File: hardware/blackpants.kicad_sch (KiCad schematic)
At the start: 26 parts, among them J1 Conn_01x08, J2 Conn_01x10, J3 Conn_ARM_SWD_TagConnect_TC203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, SW1 SW_Push, U1 STM32F042C6Ux, U11 TPSGM7227YUWQ10G

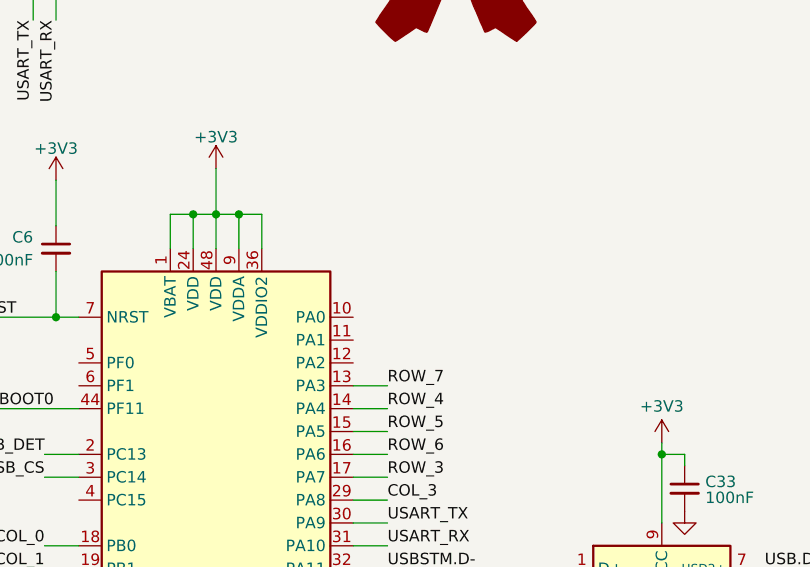
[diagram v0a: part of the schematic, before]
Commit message: Removed old readme, added files.
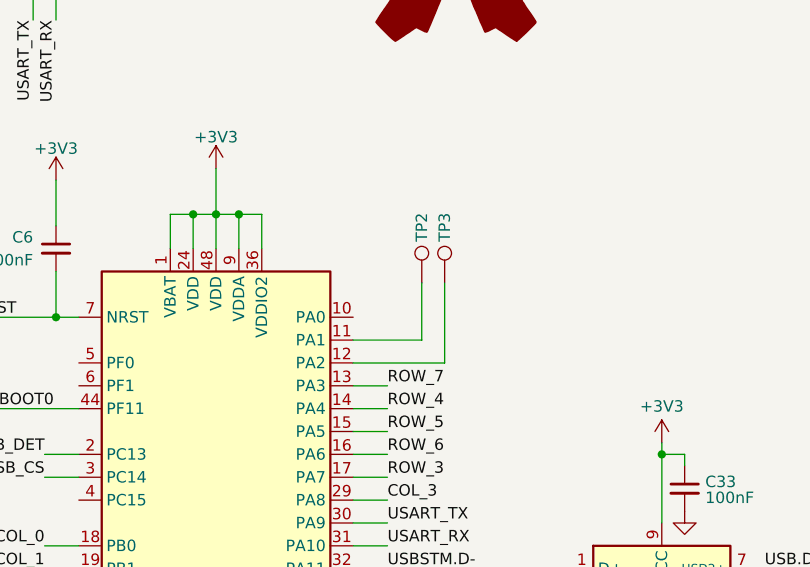
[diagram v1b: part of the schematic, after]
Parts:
- added TP2, TP3: TestPoint, TestPoint:TestPoint_Pad_1.0x1.0mm, symbol Connector:TestPoint
- C7: MPN CL05B104KB54PNC -> CL05B105KQ5NQNC
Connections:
- net at U1.11 (PA1): now also TP2.1
- net at U1.12 (PA2): now also TP3.1
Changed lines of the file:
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@@
 	(wire
 		(pts
+			(xy 156.21 88.9) (xy 156.21 80.01)
+		)
+		(stroke
+			(width 0)
+			(type default)
+		)
+	)
+	(wire
+		(pts
 			(xy 259.08 148.59) (xy 261.62 148.59)
 		)
@@
 	(wire
 		(pts
+			(xy 153.67 86.36) (xy 146.05 86.36)
+		)
+		(stroke
+			(width 0)
+			(type default)
+		)
+	)
+	(wire
+		(pts
 			(xy 190.5 114.3) (xy 200.66 114.3)
 		)
@@
 		)
 	)
+	(wire
+		(pts
+			(xy 146.05 88.9) (xy 156.21 88.9)
+		)
+		(stroke
+			(width 0)
+			(type default)
+		)
+	)
 	(bus
 		(pts
@@
 	(wire
 		(pts
+			(xy 153.67 80.01) (xy 153.67 86.36)
+		)
+		(stroke
+			(width 0)
+			(type default)
+		)
+	)
+	(wire
+		(pts
 			(xy 146.05 93.98) (xy 149.86 93.98)
 		)
@@
 	)
 	(symbol
+		(lib_id "Connector:TestPoint")
+		(at 153.67 80.01 0)
+		(unit 1)
+		(exclude_from_sim no)
+		(in_bom no)
+		(on_board yes)
+		(dnp no)
+		(property "Reference" "TP2"
+			(at 153.67 75.438 90)
+			(effects
+				(font
+					(size 1.27 1.27)
+				)
+				(justify left)
+			)
+		)
+		(property "Value" "TestPoint"
+			(at 156.21 77.9779 0)
+			(effects
+				(font
+					(size 1.27 1.27)
+				)
+				(justify left)
+				(hide yes)
+			)
+		)
+		(property "Footprint" "TestPoint:TestPoint_Pad_1.0x1.0mm"
+			(at 158.75 80.01 0)
+			(effects
+				(font
+					(size 1.27 1.27)
+				)
+				(hide yes)
+			)
+		)
+		(property "Datasheet" "~"
+			(at 158.75 80.01 0)
+			(effects
+				(font
+					(size 1.27 1.27)
+				)
+				(hide yes)
+			)
+		)
+		(property "Description" "test point"
+			(at 153.67 80.01 0)
+			(effects
+				(font
+					(size 1.27 1.27)
+				)
+				(hide yes)
+			)
+		)
+		(pin "1"
+		)
+		(instances
+			(project "blackpants"
+				(path "/d0a98fce-b133-4503-8f8a-83b2a1eed591"
+					(reference "TP2")
+					(unit 1)
+				)
+			)
+		)
+	)
+	(symbol
 		(lib_id "power:+5V")
 		(at 130.81 67.31 0)
@@
 			)
 		)
-		(property "MPN" "CL05B104KB54PNC"
+		(property "MPN" "CL05B105KQ5NQNC"
 			(at 48.26 166.37 0)
 			(effects
@@
 					(unit 1)
 				)
+			)
+		)
+	)
+	(symbol
+		(lib_id "Connector:TestPoint")
+		(at 156.21 80.01 0)
+		(unit 1)
+		(exclude_from_sim no)
+		(in_bom no)
+		(on_board yes)
+		(dnp no)
+		(property "Reference" "TP3"
+			(at 156.21 75.438 90)
+			(effects
+				(font
+					(size 1.27 1.27)
+				)
+				(justify left)
+			)
+		)
+		(property "Value" "TestPoint"
+			(at 158.75 77.9779 0)
+			(effects
+				(font
+					(size 1.27 1.27)
+				)
+				(justify left)
+				(hide yes)
+			)
+		)
+		(property "Footprint" "TestPoint:TestPoint_Pad_1.0x1.0mm"
+			(at 161.29 80.01 0)
+			(effects
+				(font
+					(size 1.27 1.27)
+				)
+				(hide yes)
+			)
+		)
+		(property "Datasheet" "~"
+			(at 161.29 80.01 0)
+			(effects
+				(font
+					(size 1.27 1.27)
+				)
+				(hide yes)
+			)
+		)
+		(property "Description" "test point"
+			(at 156.21 80.01 0)
+			(effects
+				(font
+					(size 1.27 1.27)
+				)
+				(hide yes)
+			)
+		)
+		(pin "1"
+		)
+		(instances
+			(project "blackpants"
+				(path "/d0a98fce-b133-4503-8f8a-83b2a1eed591"
+					(reference "TP3")
+					(unit 1)
+				)

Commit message: R1.0 released.
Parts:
- removed JP1: SolderJumper_2_Bridged, Jumper:SolderJumper-2_P1.3mm_Bridged_Pad1.0x1.5mm, symbol Jumper:SolderJumper_2_Bridged
- added R33: 1k, Resistor_SMD:R_0402_1005Metric, symbol Device:R
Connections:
- net +3V3: now also SW1.2
- net BOOT0: now also SW1.1, R33.2
- net GND: now also R33.1; no longer SW1.1
- net nRST: no longer SW1.2
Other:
- moved on the sheet: SW1
